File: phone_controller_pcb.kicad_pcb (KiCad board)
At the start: 2 copper layers, 3 parts, among them U1 nRF52840, Y1 ECS-320-8-37B-CKY-TR, Y2 ABS05-32.768KHZ-9-T

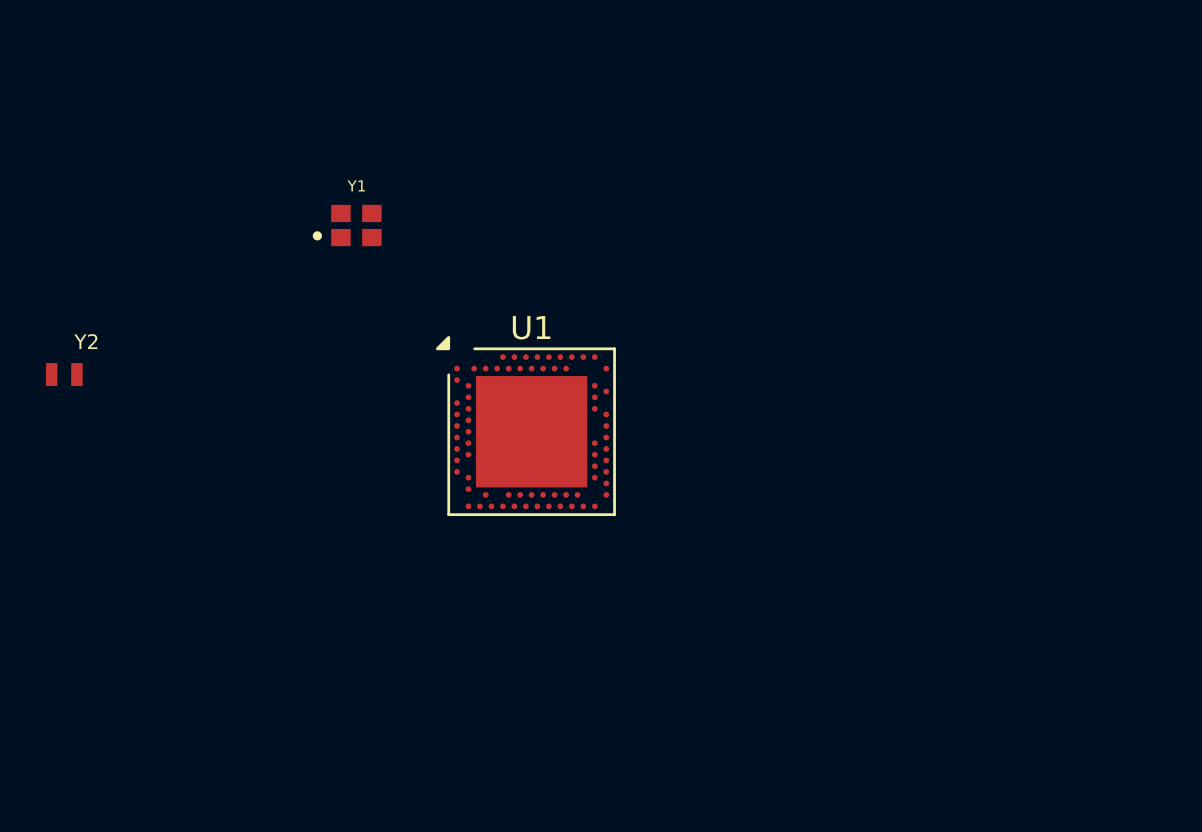
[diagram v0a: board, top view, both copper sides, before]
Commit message: Added 3d model; update capacitor values
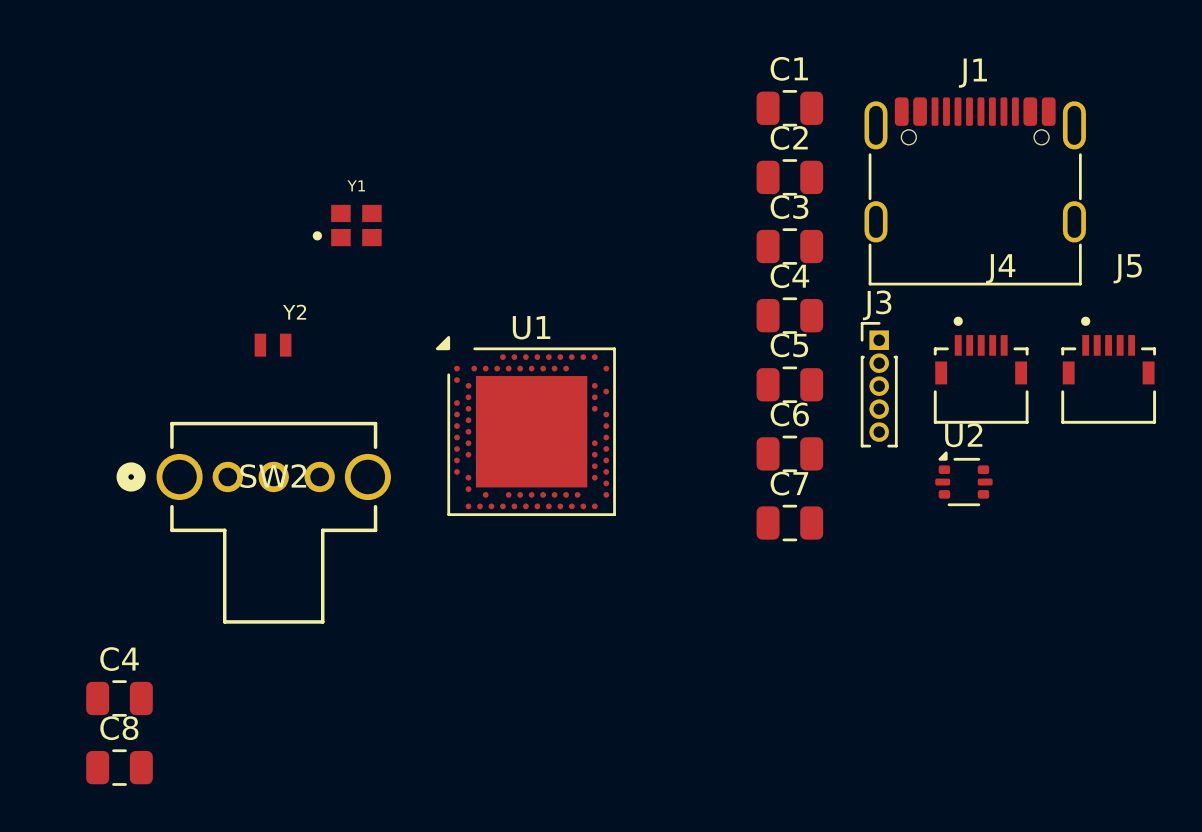
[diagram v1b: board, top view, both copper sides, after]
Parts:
- added C1: 100nF, Capacitor_SMD:C_0805_2012Metric, F.Cu at (131.4, 61.0)
- added C2: C, Capacitor_SMD:C_0805_2012Metric, F.Cu at (131.4, 64.0)
- added C3: 100pF, Capacitor_SMD:C_0805_2012Metric, F.Cu at (131.4, 67.0)
- added C4: 1uF, Capacitor_SMD:C_0805_2012Metric, F.Cu at (102.3, 86.7)
- added C4: C, Capacitor_SMD:C_0805_2012Metric, F.Cu at (131.4, 70.0)
- added C5: 820pF, Capacitor_SMD:C_0805_2012Metric, F.Cu at (131.4, 73.0)
- added C6: C, Capacitor_SMD:C_0805_2012Metric, F.Cu at (131.4, 76.0)
- added C7: 4.7uF, Capacitor_SMD:C_0805_2012Metric, F.Cu at (131.4, 79.0)
- added C8: 47nF, Capacitor_SMD:C_0805_2012Metric, F.Cu at (102.3, 89.7)
- added J1: USB_C_Receptacle_USB2.0_14P, Connector_USB:USB_C_Receptacle_G-Switch_GT-USB-7010ASV, F.Cu at (139.5, 64.9)
- added J3: Conn_01x05_Pin, Connector_PinHeader_1.00mm:PinHeader_1x05_P1.00mm_Vertical, F.Cu at (135.3, 71.1)
- added J4: Conn_01x05_Pin, 59453_052110ECHLF:AMPHENOL_59453-052110ECHLF, F.Cu at (139.8, 72.5)
- added J5: Conn_01x05_Pin, 59453_052110ECHLF:AMPHENOL_59453-052110ECHLF, F.Cu at (145.3, 72.5)
- added SW2: SW_SPDT_312, footprints:OS102011MA1QN1_CNK, F.Cu at (107.0, 77.0)
- added U2: USBLC6-2P6, Package_TO_SOT_SMD:SOT-666, F.Cu at (139.0, 77.3)
- moved Y2 9.18 mm to (108.9, 71.3)
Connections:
- U1 pad A10: unconnected-(U1-AIN5/P0.29-PadA10) -> /Y1
- U1 pad A18: unconnected-(U1-DEC2-PadA18) -> /DEC2
- U1 pad A22: Net-(U1-VDD-PadA22) -> +3.3V
- U1 pad A8: unconnected-(U1-AIN7/P0.31-PadA8) -> /Y2
- U1 pad AA24: unconnected-(U1-SWDCLK-PadAA24) -> /SWDCLK
- U1 pad AC13: unconnected-(U1-P0.18/~{RESET}-PadAC13) -> /nRESET
- U1 pad AC24: unconnected-(U1-SWDIO-PadAC24) -> /SWDIO
- U1 pad AC5: unconnected-(U1-DECUSB-PadAC5) -> /DECUSB
- U1 pad AD14: Net-(U1-VDD-PadA22) -> +3.3V
- U1 pad AD2: unconnected-(U1-VBUS-PadAD2) -> +5V
- U1 pad AD23: Net-(U1-VDD-PadA22) -> +3.3V
- U1 pad AD4: unconnected-(U1-D--PadAD4) -> /USB_D-
- U1 pad AD6: unconnected-(U1-D+-PadAD6) -> /USB_D+
- U1 pad B1: Net-(U1-VDD-PadA22) -> +3.3V
- U1 pad B11: unconnected-(U1-AIN4/P0.28-PadB11) -> /X1
- U1 pad B5: unconnected-(U1-DEC4-PadB5) -> /DEC4_6
- U1 pad B7: Net-(U1-VSS-PadB7) -> GND
- U1 pad B9: unconnected-(U1-AIN6/P0.30-PadB9) -> /X2
- U1 pad C1: unconnected-(U1-DEC1-PadC1) -> /DEC1
- U1 pad D23: unconnected-(U1-DEC3-PadD23) -> /DEC3
- U1 pad E24: unconnected-(U1-DEC6-PadE24) -> /DEC4_6
- U1 pad EP: Net-(U1-VSS-PadB7) -> GND
- U1 pad F23: unconnected-(U1-VSS_PA-PadF23) -> GND
- U1 pad G1: unconnected-(U1-P0.26-PadG1) -> /S1
- U1 pad H2: unconnected-(U1-P0.27-PadH2) -> /S2
- U1 pad N24: unconnected-(U1-DEC5-PadN24) -> /DEC5
- U1 pad W1: Net-(U1-VDD-PadA22) -> +3.3V
- U1 pad Y2: unconnected-(U1-VDDH-PadY2) -> +3.3V
